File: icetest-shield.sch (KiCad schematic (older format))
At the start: 7 parts

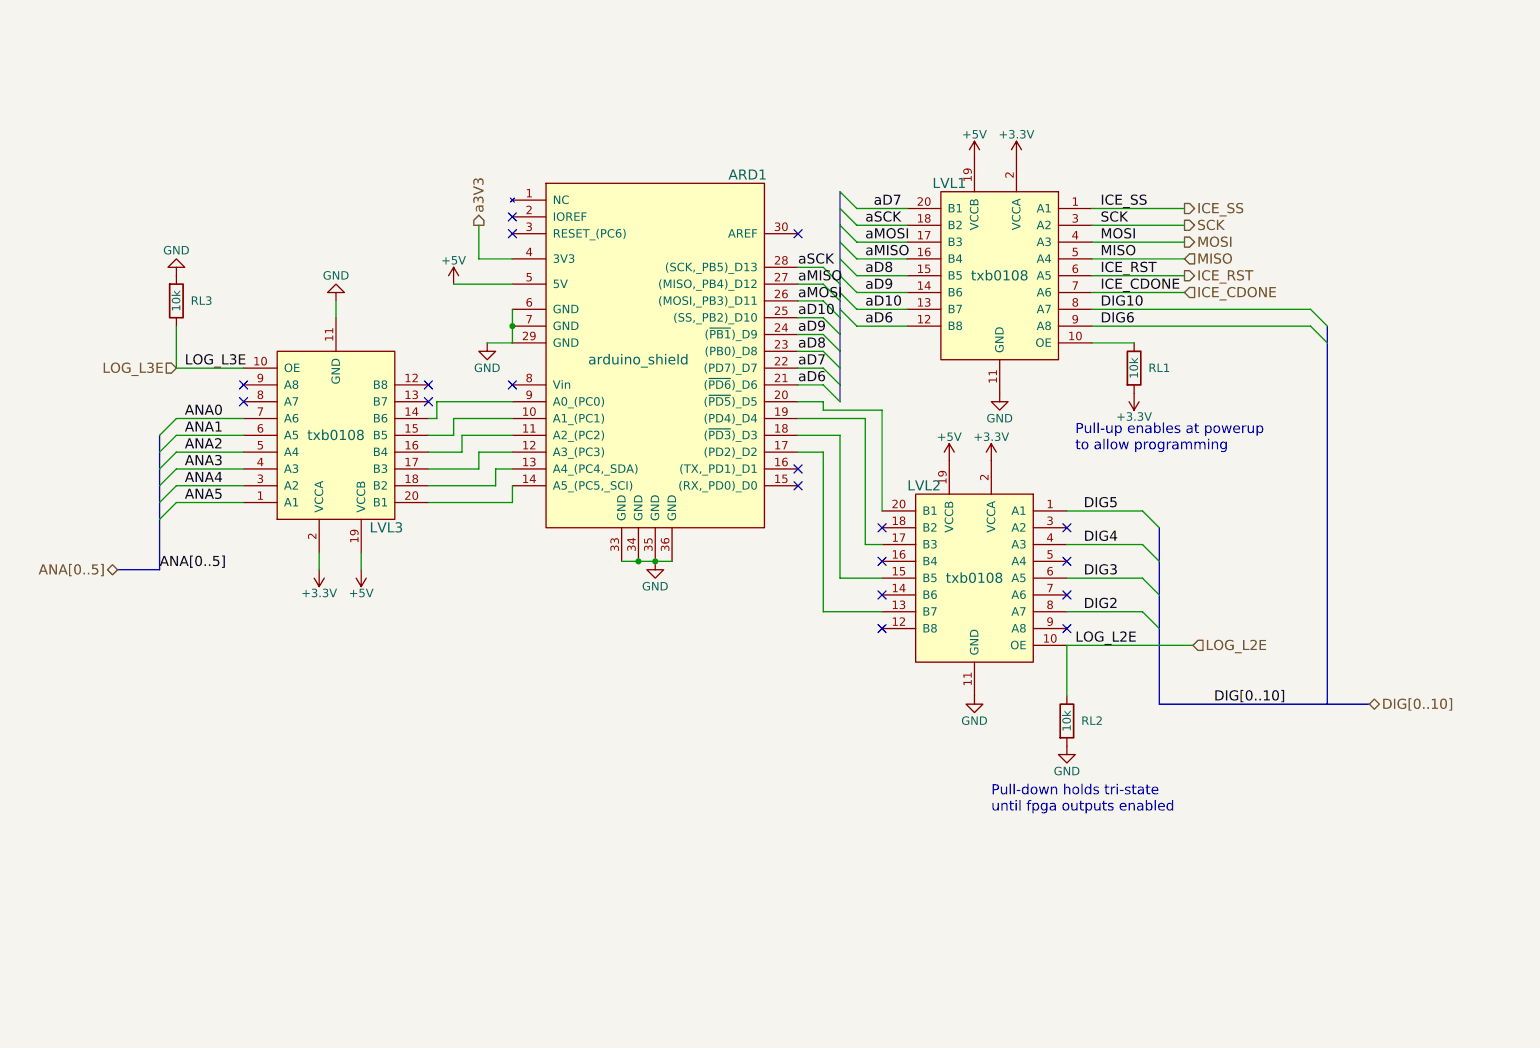
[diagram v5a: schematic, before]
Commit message: switch level shifter
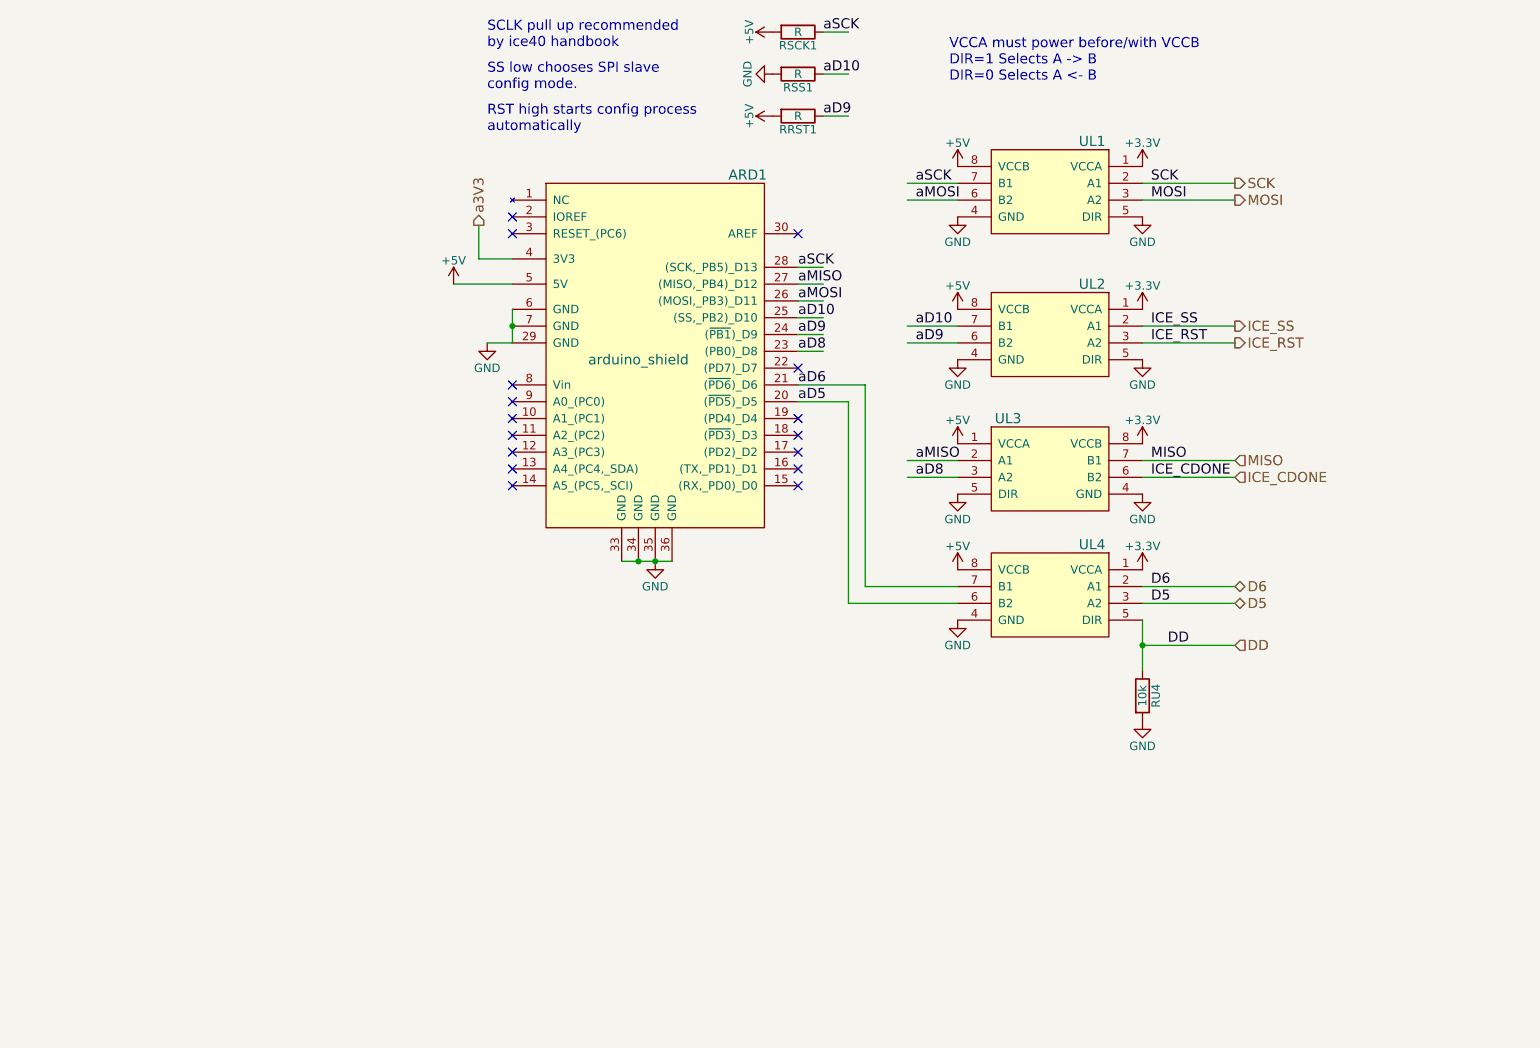
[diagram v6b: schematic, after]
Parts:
- removed LVL1, LVL2, LVL3: txb0108, local:PSO_20, symbol txb0108
- removed RL1, RL2, RL3: 10k, Resistors_SMD:R_0603_HandSoldering, symbol R
- added RRST1, RSCK1, RSS1: R, symbol R
- added RU4: 10k, symbol R
- added UL1, UL2, UL3, UL4: sn74lvc2t45, symbol sn74lvc2t45
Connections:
- net labels added: D5, D6, DD, aD5
- net labels removed: ANA0, ANA1, ANA2, ANA3, ANA4, ANA5, ANA[0..5], DIG10, DIG2, DIG3, DIG4, DIG5, DIG6, DIG[0..10], LOG_L2E, LOG_L3E, aD7
- wire segments 78 -> 37
- no-connect marks 18 -> 16
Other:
- note added: "RST high starts config process\nautomatically"
- note added: "SCLK pull up recommended\nby ice40 handbook"
- note added: "SS low chooses SPI slave\nconfig mode."
- note added: "VCCA must power before/with VCCB\nDIR=1 Selects A -> B\nDIR=0 Selects A <- B"
- note removed: "Pull-down holds tri-state\nuntil fpga outputs enabled"
- note removed: "Pull-up enables at powerup\nto allow programming"

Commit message: redo layout
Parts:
- added RU3: 10k, Resistors_SMD:R_0603_HandSoldering, symbol R
- RRST1, RSCK1, RSS1: value R -> 10k; footprint (none) -> Resistors_SMD:R_0603_HandSoldering
- RU4: footprint (none) -> Resistors_SMD:R_0603_HandSoldering
- UL1, UL2, UL3, UL4: footprint (none) -> local:VSSOP-8
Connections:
- wire segments 37 -> 39
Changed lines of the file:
@@
 Title "Arduino shield with iCE40 FPGA"
 Date ""
-Rev "0"
+Rev "2"
 Comp "mdavidsaver@gmail.com"
 Comment1 ""
@@
 F 0 "UL1" H 7200 2800 60  0000 C CNN
 F 1 "sn74lvc2t45" H 7450 3200 60  0001 C CNN
-F 2 "" H 7700 2350 60  0000 C CNN
+F 2 "local:VSSOP-8" H 7700 2350 60  0001 C CNN
 F 3 "" H 7700 2350 60  0000 C CNN
 	1    7450 2500
@@
 F 0 "UL2" H 7200 3650 60  0000 C CNN
 F 1 "sn74lvc2t45" H 7450 4050 60  0001 C CNN
-F 2 "" H 7700 3200 60  0000 C CNN
+F 2 "local:VSSOP-8" H 7700 3200 60  0001 C CNN
 F 3 "" H 7700 3200 60  0000 C CNN
 	1    7450 3350
@@
 F 0 "UL3" H 7200 4450 60  0000 C CNN
 F 1 "sn74lvc2t45" H 7450 4850 60  0001 C CNN
-F 2 "" H 7700 4000 60  0000 C CNN
+F 2 "local:VSSOP-8" H 7700 4000 60  0001 C CNN
 F 3 "" H 7700 4000 60  0000 C CNN
 	1    7450 4150
-	1    0    0    -1
+	-1   0    0    -1
 $EndComp
 $Comp
@@
 $EndComp
 $Comp
-L GND #PWR063
-U 1 1 57F9C251
-P 8000 4300
-F 0 "#PWR063" H 8000 4050 50  0001 C CNN
-F 1 "GND" H 8000 4150 50  0000 C CNN
-F 2 "" H 8000 4300 50  0000 C CNN
-F 3 "" H 8000 4300 50  0000 C CNN
-	1    8000 4300
-	-1   0    0    -1
-$EndComp
-$Comp
-L +3.3V #PWR064
+L +3.3V #PWR063
 U 1 1 57F9C281
 P 8000 4750
-F 0 "#PWR064" H 8000 4600 50  0001 C CNN
+F 0 "#PWR063" H 8000 4600 50  0001 C CNN
 F 1 "+3.3V" H 8000 4890 50  0000 C CNN
 F 2 "" H 8000 4750 50  0000 C CNN
@@
 $EndComp
 $Comp
-L +5V #PWR065
+L +5V #PWR064
 U 1 1 57F9C287
 P 6900 4750
-F 0 "#PWR065" H 6900 4600 50  0001 C CNN
+F 0 "#PWR064" H 6900 4600 50  0001 C CNN
 F 1 "+5V" H 6900 4890 50  0000 C CNN
 F 2 "" H 6900 4750 50  0000 C CNN
@@
 F 0 "UL4" H 7200 5200 60  0000 C CNN
 F 1 "sn74lvc2t45" H 7450 5600 60  0001 C CNN
-F 2 "" H 7700 4750 60  0000 C CNN
+F 2 "local:VSSOP-8" H 7700 4750 60  0001 C CNN
 F 3 "" H 7700 4750 60  0000 C CNN
 	1    7450 4900
@@
 $EndComp
 $Comp
-L GND #PWR066
+L GND #PWR065
 U 1 1 57F9C293
 P 6900 5050
-F 0 "#PWR066" H 6900 4800 50  0001 C CNN
+F 0 "#PWR065" H 6900 4800 50  0001 C CNN
 F 1 "GND" H 6900 4900 50  0000 C CNN
 F 2 "" H 6900 5050 50  0000 C CNN
@@
 $EndComp
 $Comp
-L GND #PWR067
+L GND #PWR066
 U 1 1 57F9C299
 P 8000 5650
-F 0 "#PWR067" H 8000 5400 50  0001 C CNN
+F 0 "#PWR066" H 8000 5400 50  0001 C CNN
 F 1 "GND" H 8000 5500 50  0000 C CNN
 F 2 "" H 8000 5650 50  0000 C CNN
@@
 P 5950 1550
 F 0 "RSCK1" V 6030 1550 50  0000 C CNN
-F 1 "R" V 5950 1550 50  0000 C CNN
-F 2 "" V 5880 1550 50  0000 C CNN
+F 1 "10k" V 5950 1550 50  0000 C CNN
+F 2 "Resistors_SMD:R_0603_HandSoldering" V 5880 1550 50  0001 C CNN
 F 3 "" H 5950 1550 50  0000 C CNN
 	1    5950 1550
@@
 P 5950 1800
 F 0 "RSS1" V 6030 1800 50  0000 C CNN
-F 1 "R" V 5950 1800 50  0000 C CNN
-F 2 "" V 5880 1800 50  0000 C CNN
+F 1 "10k" V 5950 1800 50  0000 C CNN
+F 2 "Resistors_SMD:R_0603_HandSoldering" V 5880 1800 50  0001 C CNN
 F 3 "" H 5950 1800 50  0000 C CNN
 	1    5950 1800
@@
 $EndComp
 $Comp
-L GND #PWR068
+L GND #PWR067
 U 1 1 57FA17AB
 P 5800 1800
-F 0 "#PWR068" H 5800 1550 50  0001 C CNN
+F 0 "#PWR067" H 5800 1550 50  0001 C CNN
 F 1 "GND" H 5800 1650 50  0000 C CNN
 F 2 "" H 5800 1800 50  0000 C CNN
@@
 P 5950 2050
 F 0 "RRST1" V 6030 2050 50  0000 C CNN
-F 1 "R" V 5950 2050 50  0000 C CNN
-F 2 "" V 5880 2050 50  0000 C CNN
+F 1 "10k" V 5950 2050 50  0000 C CNN
+F 2 "Resistors_SMD:R_0603_HandSoldering" V 5880 2050 50  0001 C CNN
 F 3 "" H 5950 2050 50  0000 C CNN
 	1    5950 2050
@@
 F 0 "RU4" V 8080 5500 50  0000 C CNN
 F 1 "10k" V 8000 5500 50  0000 C CNN
-F 2 "" V 7930 5500 50  0000 C CNN
+F 2 "Resistors_SMD:R_0603_HandSoldering" V 7930 5500 50  0001 C CNN
 F 3 "" H 8000 5500 50  0000 C CNN
 	1    8000 5500
@@
 DD
 $Comp
-L +5V #PWR069
+L +5V #PWR068
 U 1 1 57FC7EF2
 P 5800 1550
-F 0 "#PWR069" H 5800 1400 50  0001 C CNN
+F 0 "#PWR068" H 5800 1400 50  0001 C CNN
 F 1 "+5V" H 5800 1690 50  0000 C CNN
 F 2 "" H 5800 1550 50  0000 C CNN
@@
 $EndComp
 $Comp
-L +5V #PWR070
+L +5V #PWR069
 U 1 1 57FC7F18
 P 5800 2050
-F 0 "#PWR070" H 5800 1900 50  0001 C CNN
+F 0 "#PWR069" H 5800 1900 50  0001 C CNN
 F 1 "+5V" H 5800 2190 50  0000 C CNN
 F 2 "" H 5800 2050 50  0000 C CNN
@@
 	0    -1   -1   0
 $EndComp
+$Comp
+L R RU3
+U 1 1 57FAE023
+P 8250 4300
+F 0 "RU3" V 8330 4300 50  0000 C CNN
+F 1 "10k" V 8250 4300 50  0000 C CNN
+F 2 "Resistors_SMD:R_0603_HandSoldering" V 8180 4300 50  0001 C CNN
+F 3 "" H 8250 4300 50  0000 C CNN
+	1    8250 4300
+	0    1    1    0
+$EndComp
+Wire Wire Line
+	8000 4300 8100 4300
+Wire Wire Line
+	8400 4300 8550 4300
+$Comp
+L +3.3V #PWR070
+U 1 1 57FAE2AA
+P 8550 4300
+F 0 "#PWR070" H 8550 4150 50  0001 C CNN
+F 1 "+3.3V" H 8550 4440 50  0000 C CNN
+F 2 "" H 8550 4300 50  0000 C CNN
+F 3 "" H 8550 4300 50  0000 C CNN
+	1    8550 4300
+	1    0    0    1
+$EndComp
 $EndSCHEMATC

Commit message: more layout
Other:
- note added: "VCCA must power before/with VCCB\nDIR=1 Selects B <- A\nDIR=0 Selects B -> A"
- note removed: "VCCA must power before/with VCCB\nDIR=1 Selects A -> B\nDIR=0 Selects A <- B"
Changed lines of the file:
@@
 $EndComp
 $Comp
-L GND #PWR049
+L GND #PWR050
 U 1 1 578B7F2F
 P 4100 3400
-F 0 "#PWR049" H 4100 3150 50  0001 C CNN
+F 0 "#PWR050" H 4100 3150 50  0001 C CNN
 F 1 "GND" H 4100 3250 50  0000 C CNN
 F 2 "" H 4100 3400 50  0000 C CNN
@@
 $EndComp
 $Comp
-L +5V #PWR050
+L +5V #PWR051
 U 1 1 578B7F35
 P 3900 3050
-F 0 "#PWR050" H 3900 2900 50  0001 C CNN
+F 0 "#PWR051" H 3900 2900 50  0001 C CNN
 F 1 "+5V" H 3900 3190 50  0000 C CNN
 F 2 "" H 3900 3050 50  0000 C CNN
@@
 NoConn ~ 5950 2750
 $Comp
-L +3.3V #PWR051
+L +3.3V #PWR052
 U 1 1 578B7F8A
 P 8000 2350
-F 0 "#PWR051" H 8000 2200 50  0001 C CNN
+F 0 "#PWR052" H 8000 2200 50  0001 C CNN
 F 1 "+3.3V" H 8000 2490 50  0000 C CNN
 F 2 "" H 8000 2350 50  0000 C CNN
@@
 $EndComp
 $Comp
-L +5V #PWR052
+L +5V #PWR053
 U 1 1 578B7F90
 P 6900 2350
-F 0 "#PWR052" H 6900 2200 50  0001 C CNN
+F 0 "#PWR053" H 6900 2200 50  0001 C CNN
 F 1 "+5V" H 6900 2490 50  0000 C CNN
 F 2 "" H 6900 2350 50  0000 C CNN
@@
 ICE_CDONE
 $Comp
-L GND #PWR053
+L GND #PWR054
 U 1 1 5793C5E6
 P 5100 4700
-F 0 "#PWR053" H 5100 4450 50  0001 C CNN
+F 0 "#PWR054" H 5100 4450 50  0001 C CNN
 F 1 "GND" H 5100 4550 50  0000 C CNN
 F 2 "" H 5100 4700 50  0000 C CNN
@@
 $EndComp
 $Comp
-L GND #PWR054
+L GND #PWR055
 U 1 1 57F9B00B
 P 6900 2650
-F 0 "#PWR054" H 6900 2400 50  0001 C CNN
+F 0 "#PWR055" H 6900 2400 50  0001 C CNN
 F 1 "GND" H 6900 2500 50  0000 C CNN
 F 2 "" H 6900 2650 50  0000 C CNN
@@
 $EndComp
 Text Notes 6850 1850 0    60   ~ 0
-VCCA must power before/with VCCB\nDIR=1 Selects A -> B\nDIR=0 Selects A <- B
-$Comp
-L GND #PWR055
+VCCA must power before/with VCCB\nDIR=1 Selects B <- A\nDIR=0 Selects B -> A
+$Comp
+L GND #PWR056
 U 1 1 57F9C120
 P 8000 2650
-F 0 "#PWR055" H 8000 2400 50  0001 C CNN
+F 0 "#PWR056" H 8000 2400 50  0001 C CNN
 F 1 "GND" H 8000 2500 50  0000 C CNN
 F 2 "" H 8000 2650 50  0000 C CNN
@@
 $EndComp
 $Comp
-L +3.3V #PWR056
+L +3.3V #PWR057
 U 1 1 57F9C181
 P 8000 3200
-F 0 "#PWR056" H 8000 3050 50  0001 C CNN
+F 0 "#PWR057" H 8000 3050 50  0001 C CNN
 F 1 "+3.3V" H 8000 3340 50  0000 C CNN
 F 2 "" H 8000 3200 50  0000 C CNN
@@
 $EndComp
 $Comp
-L +5V #PWR057
+L +5V #PWR058
 U 1 1 57F9C187
 P 6900 3200
-F 0 "#PWR057" H 6900 3050 50  0001 C CNN
+F 0 "#PWR058" H 6900 3050 50  0001 C CNN
 F 1 "+5V" H 6900 3340 50  0000 C CNN
 F 2 "" H 6900 3200 50  0000 C CNN
@@
 $EndComp
 $Comp
-L GND #PWR058
+L GND #PWR059
 U 1 1 57F9C193
 P 6900 3500
-F 0 "#PWR058" H 6900 3250 50  0001 C CNN
+F 0 "#PWR059" H 6900 3250 50  0001 C CNN
 F 1 "GND" H 6900 3350 50  0000 C CNN
 F 2 "" H 6900 3500 50  0000 C CNN
@@
 $EndComp
 $Comp
-L GND #PWR059
+L GND #PWR060
 U 1 1 57F9C199
 P 8000 3500
-F 0 "#PWR059" H 8000 3250 50  0001 C CNN
+F 0 "#PWR060" H 8000 3250 50  0001 C CNN
 F 1 "GND" H 8000 3350 50  0000 C CNN
 F 2 "" H 8000 3500 50  0000 C CNN
@@
 $EndComp
 $Comp
-L +3.3V #PWR060
+L +3.3V #PWR061
 U 1 1 57F9C239
 P 8000 4000
-F 0 "#PWR060" H 8000 3850 50  0001 C CNN
+F 0 "#PWR061" H 8000 3850 50  0001 C CNN
 F 1 "+3.3V" H 8000 4140 50  0000 C CNN
 F 2 "" H 8000 4000 50  0000 C CNN
@@
 $EndComp
 $Comp
-L +5V #PWR061
+L +5V #PWR062
 U 1 1 57F9C23F
 P 6900 4000
-F 0 "#PWR061" H 6900 3850 50  0001 C CNN
+F 0 "#PWR062" H 6900 3850 50  0001 C CNN
 F 1 "+5V" H 6900 4140 50  0000 C CNN
 F 2 "" H 6900 4000 50  0000 C CNN
@@
 $EndComp
 $Comp
-L GND #PWR062
+L GND #PWR063
 U 1 1 57F9C24B
 P 6900 4300
-F 0 "#PWR062" H 6900 4050 50  0001 C CNN
+F 0 "#PWR063" H 6900 4050 50  0001 C CNN
 F 1 "GND" H 6900 4150 50  0000 C CNN
 F 2 "" H 6900 4300 50  0000 C CNN
@@
 $EndComp
 $Comp
-L +3.3V #PWR063
+L +3.3V #PWR064
 U 1 1 57F9C281
 P 8000 4750
-F 0 "#PWR063" H 8000 4600 50  0001 C CNN
+F 0 "#PWR064" H 8000 4600 50  0001 C CNN
 F 1 "+3.3V" H 8000 4890 50  0000 C CNN
 F 2 "" H 8000 4750 50  0000 C CNN
@@
 $EndComp
 $Comp
-L +5V #PWR064
+L +5V #PWR065
 U 1 1 57F9C287
 P 6900 4750
-F 0 "#PWR064" H 6900 4600 50  0001 C CNN
+F 0 "#PWR065" H 6900 4600 50  0001 C CNN
 F 1 "+5V" H 6900 4890 50  0000 C CNN
 F 2 "" H 6900 4750 50  0000 C CNN
@@
 $EndComp
 $Comp
-L GND #PWR065
+L GND #PWR066
 U 1 1 57F9C293
 P 6900 5050
-F 0 "#PWR065" H 6900 4800 50  0001 C CNN
+F 0 "#PWR066" H 6900 4800 50  0001 C CNN
 F 1 "GND" H 6900 4900 50  0000 C CNN
 F 2 "" H 6900 5050 50  0000 C CNN
@@
 $EndComp
 $Comp
-L GND #PWR066
+L GND #PWR067
 U 1 1 57F9C299
 P 8000 5650
-F 0 "#PWR066" H 8000 5400 50  0001 C CNN
+F 0 "#PWR067" H 8000 5400 50  0001 C CNN
 F 1 "GND" H 8000 5500 50  0000 C CNN
 F 2 "" H 8000 5650 50  0000 C CNN
@@
 $EndComp
 $Comp
-L GND #PWR067
+L GND #PWR068
 U 1 1 57FA17AB
 P 5800 1800
-F 0 "#PWR067" H 5800 1550 50  0001 C CNN
+F 0 "#PWR068" H 5800 1550 50  0001 C CNN
 F 1 "GND" H 5800 1650 50  0000 C CNN
 F 2 "" H 5800 1800 50  0000 C CNN
@@
 DD
 $Comp
-L +5V #PWR068
+L +5V #PWR069
 U 1 1 57FC7EF2
 P 5800 1550
-F 0 "#PWR068" H 5800 1400 50  0001 C CNN
+F 0 "#PWR069" H 5800 1400 50  0001 C CNN
 F 1 "+5V" H 5800 1690 50  0000 C CNN
 F 2 "" H 5800 1550 50  0000 C CNN
@@
 $EndComp
 $Comp
-L +5V #PWR069
+L +5V #PWR070
 U 1 1 57FC7F18
 P 5800 2050
-F 0 "#PWR069" H 5800 1900 50  0001 C CNN
+F 0 "#PWR070" H 5800 1900 50  0001 C CNN
 F 1 "+5V" H 5800 2190 50  0000 C CNN
 F 2 "" H 5800 2050 50  0000 C CNN
@@
 	8400 4300 8550 4300
 $Comp
-L +3.3V #PWR070
+L +3.3V #PWR071
 U 1 1 57FAE2AA
 P 8550 4300
-F 0 "#PWR070" H 8550 4150 50  0001 C CNN
+F 0 "#PWR071" H 8550 4150 50  0001 C CNN
 F 1 "+3.3V" H 8550 4440 50  0000 C CNN
 F 2 "" H 8550 4300 50  0000 C CNN
